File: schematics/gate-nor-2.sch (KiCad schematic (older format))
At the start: 4 parts, among them Q1 NPN

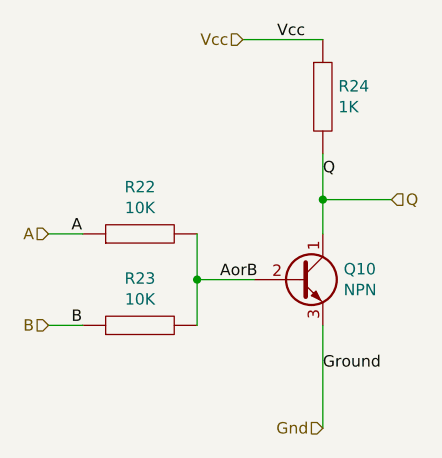
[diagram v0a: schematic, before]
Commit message: ALU is sketched but has functional defects
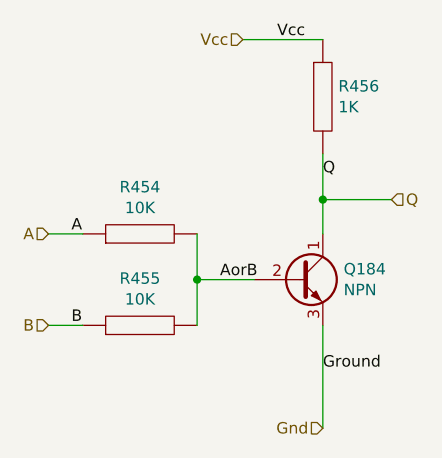
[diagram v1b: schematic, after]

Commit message: Adds a netlist "optimizer" which shortens names for better output parsing
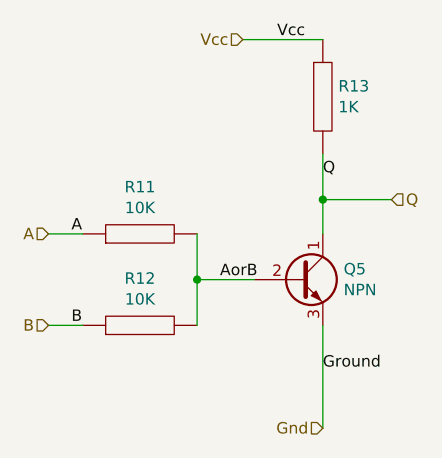
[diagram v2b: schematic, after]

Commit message: Adds some tests for and-2, nor-2, nor-3
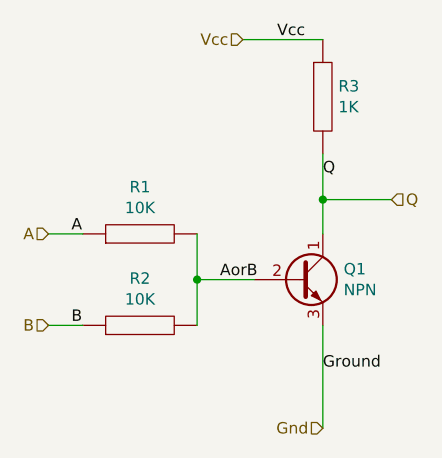
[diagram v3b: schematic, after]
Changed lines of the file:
@@
 EESchema Schematic File Version 4
-LIBS:gate-xor-2-test-cache
+LIBS:gate-and-2-test-cache
 EELAYER 26 0
 EELAYER END
 $Descr A4 11693 8268
 encoding utf-8
-Sheet 3 8
+Sheet 3 5
 Title ""
 Date ""
@@
 AR Path="/5C4EA7CD/5C4EEBEC/5C3B3FFC/5C34B066/5C561AB5" Ref="R?"  Part="1"
 AR Path="/5C4EA7CD/5C4EEBEC/5C3B3FFC/5C34B0D4/5C561AB5" Ref="R?"  Part="1"
-AR Path="/5C4DE58B/5C4DE622/5C561AB5" Ref="R3"  Part="1"
-AR Path="/5C4DE58B/5C4DE6C4/5C561AAA/5C561AB5" Ref="R6"  Part="1"
-AR Path="/5C4DE58B/5C4DE709/5C561AB5" Ref="R13"  Part="1"
-F 0 "R13" H 6068 3496 50  0000 L CNN
+AR Path="/5C4DE58B/5C4DE622/5C561AB5" Ref="R?"  Part="1"
+AR Path="/5C4DE58B/5C4DE6C4/5C561AAA/5C561AB5" Ref="R?"  Part="1"
+AR Path="/5C4DE58B/5C4DE709/5C561AB5" Ref="R?"  Part="1"
+AR Path="/5C3FE316/5C561AAA/5C561AB5" Ref="R3"  Part="1"
+F 0 "R3" H 6068 3496 50  0000 L CNN
 F 1 "1K" H 6068 3405 50  0000 L CNN
 F 2 "" H 6000 3450 50  0001 C CNN
@@
 AR Path="/5C4EA7CD/5C4EEBEC/5C3B3FFC/5C34B066/5C42F129" Ref="R?"  Part="1"
 AR Path="/5C4EA7CD/5C4EEBEC/5C3B3FFC/5C34B0D4/5C42F129" Ref="R?"  Part="1"
-AR Path="/5C4DE58B/5C4DE622/5C42F129" Ref="R1"  Part="1"
-AR Path="/5C4DE58B/5C4DE6C4/5C561AAA/5C42F129" Ref="R4"  Part="1"
-AR Path="/5C4DE58B/5C4DE709/5C42F129" Ref="R11"  Part="1"
-F 0 "R11" V 5405 4050 50  0000 C CNN
+AR Path="/5C4DE58B/5C4DE622/5C42F129" Ref="R?"  Part="1"
+AR Path="/5C4DE58B/5C4DE6C4/5C561AAA/5C42F129" Ref="R?"  Part="1"
+AR Path="/5C4DE58B/5C4DE709/5C42F129" Ref="R?"  Part="1"
+AR Path="/5C3FE316/5C561AAA/5C42F129" Ref="R1"  Part="1"
+F 0 "R1" V 5405 4050 50  0000 C CNN
 F 1 "10K" V 5314 4050 50  0000 C CNN
 F 2 "" H 5200 4050 50  0001 C CNN
@@
 AR Path="/5C4EA7CD/5C4EEBEC/5C3B3FFC/5C34B066/5C42F12A" Ref="R?"  Part="1"
 AR Path="/5C4EA7CD/5C4EEBEC/5C3B3FFC/5C34B0D4/5C42F12A" Ref="R?"  Part="1"
-AR Path="/5C4DE58B/5C4DE622/5C42F12A" Ref="R2"  Part="1"
-AR Path="/5C4DE58B/5C4DE6C4/5C561AAA/5C42F12A" Ref="R5"  Part="1"
-AR Path="/5C4DE58B/5C4DE709/5C42F12A" Ref="R12"  Part="1"
-F 0 "R12" V 5405 4450 50  0000 C CNN
+AR Path="/5C4DE58B/5C4DE622/5C42F12A" Ref="R?"  Part="1"
+AR Path="/5C4DE58B/5C4DE6C4/5C561AAA/5C42F12A" Ref="R?"  Part="1"
+AR Path="/5C4DE58B/5C4DE709/5C42F12A" Ref="R?"  Part="1"
+AR Path="/5C3FE316/5C561AAA/5C42F12A" Ref="R2"  Part="1"
+F 0 "R2" V 5405 4450 50  0000 C CNN
 F 1 "10K" V 5314 4450 50  0000 C CNN
 F 2 "" H 5200 4450 50  0001 C CNN
@@
 AR Path="/5C4EA7CD/5C4EEBEC/5C3B3FFC/5C34B066/5C561AC1" Ref="Q?"  Part="1"
 AR Path="/5C4EA7CD/5C4EEBEC/5C3B3FFC/5C34B0D4/5C561AC1" Ref="Q?"  Part="1"
-AR Path="/5C4DE58B/5C4DE622/5C561AC1" Ref="Q1"  Part="1"
-AR Path="/5C4DE58B/5C4DE6C4/5C561AAA/5C561AC1" Ref="Q2"  Part="1"
-AR Path="/5C4DE58B/5C4DE709/5C561AC1" Ref="Q5"  Part="1"
-F 0 "Q5" H 6091 4296 50  0000 L CNN
+AR Path="/5C4DE58B/5C4DE622/5C561AC1" Ref="Q?"  Part="1"
+AR Path="/5C4DE58B/5C4DE6C4/5C561AAA/5C561AC1" Ref="Q?"  Part="1"
+AR Path="/5C4DE58B/5C4DE709/5C561AC1" Ref="Q?"  Part="1"
+AR Path="/5C3FE316/5C561AAA/5C561AC1" Ref="Q1"  Part="1"
+F 0 "Q1" H 6091 4296 50  0000 L CNN
 F 1 "NPN" H 6091 4205 50  0000 L CNN
 F 2 "Package_TO_SOT_THT:TO-92_Inline" H 6100 4175 50  0001 L CIN

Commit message: Test output is a bit more functional... ALU still has defects
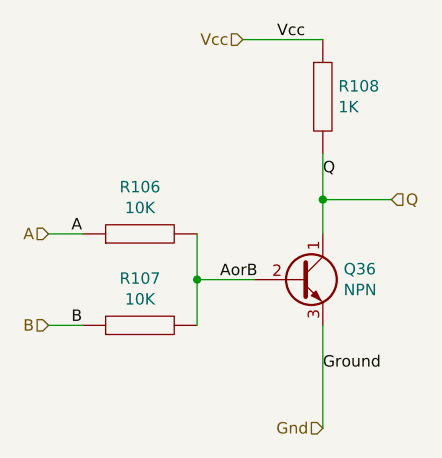
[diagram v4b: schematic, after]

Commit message: More testing.  Trying to find defect in ALU
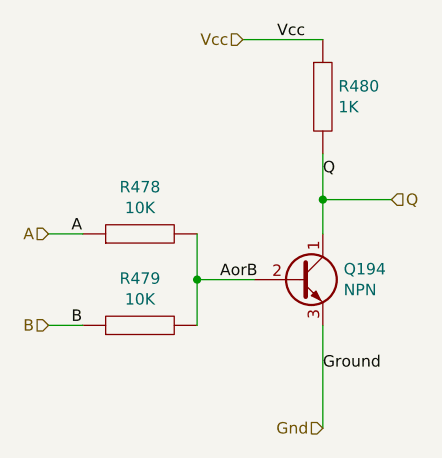
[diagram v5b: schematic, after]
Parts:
- renumbered Q1 to Q149, R1 to R349, R2 to R350, R3 to R351

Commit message: ALU appears to work as expected
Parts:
- renumbered R351 to R349, R349 to R350, R350 to R351

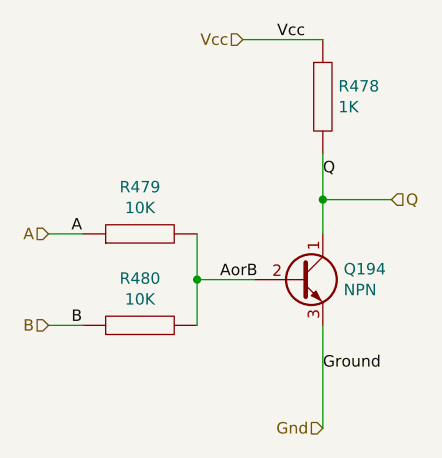
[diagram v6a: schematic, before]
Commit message: Can now automate transient analysis
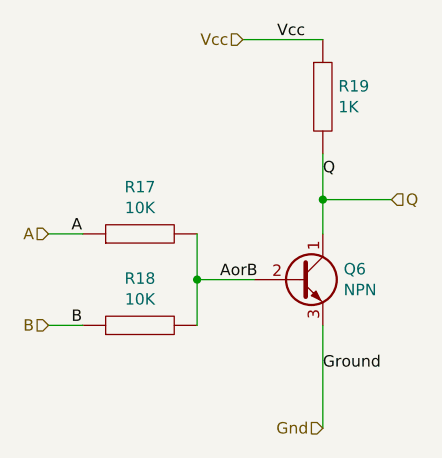
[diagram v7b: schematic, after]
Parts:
- Q1: renamed from Q149; footprint Package_TO_SOT_THT:TO-92_Inline -> Socket_Strips:Socket_Strip_Straight_1x03_Pitch1.27mm
- R1: renamed from R350; footprint (none) -> Resistors_THT:R_Axial_DIN0207_L6.3mm_D2.5mm_P10.16mm_Horizontal
- R2: renamed from R351; footprint (none) -> Resistors_THT:R_Axial_DIN0207_L6.3mm_D2.5mm_P10.16mm_Horizontal
- R3: renamed from R349; footprint (none) -> Resistors_THT:R_Axial_DIN0207_L6.3mm_D2.5mm_P10.16mm_Horizontal
